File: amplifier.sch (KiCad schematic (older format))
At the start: 3 parts, among them U401 AD8426ACPZ-R7

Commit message: placed digital gnd plane
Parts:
- C401, C402: footprint Capacitor_SMD:C_0805_2012Metric_Pad1.15x1.40mm_HandSolder -> Capacitor_SMD:C_0603_1608Metric_Pad1.05x0.95mm_HandSolder
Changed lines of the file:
@@
 F 0 "C401" H 3615 4846 50  0000 L CNN
 F 1 "0.1uF" H 3615 4755 50  0000 L CNN
-F 2 "Capacitor_SMD:C_0805_2012Metric_Pad1.15x1.40mm_HandSolder" H 3538 4650 50  0001 C CNN
+F 2 "Capacitor_SMD:C_0603_1608Metric_Pad1.05x0.95mm_HandSolder" H 3538 4650 50  0001 C CNN
 F 3 "~" H 3500 4800 50  0001 C CNN
 	1    3500 4800
@@
 F 0 "C402" H 4265 4846 50  0000 L CNN
 F 1 "10uF" H 4265 4755 50  0000 L CNN
-F 2 "Capacitor_SMD:C_0805_2012Metric_Pad1.15x1.40mm_HandSolder" H 4188 4650 50  0001 C CNN
+F 2 "Capacitor_SMD:C_0603_1608Metric_Pad1.05x0.95mm_HandSolder" H 4188 4650 50  0001 C CNN
 F 3 "~" H 4150 4800 50  0001 C CNN
 	1    4150 4800

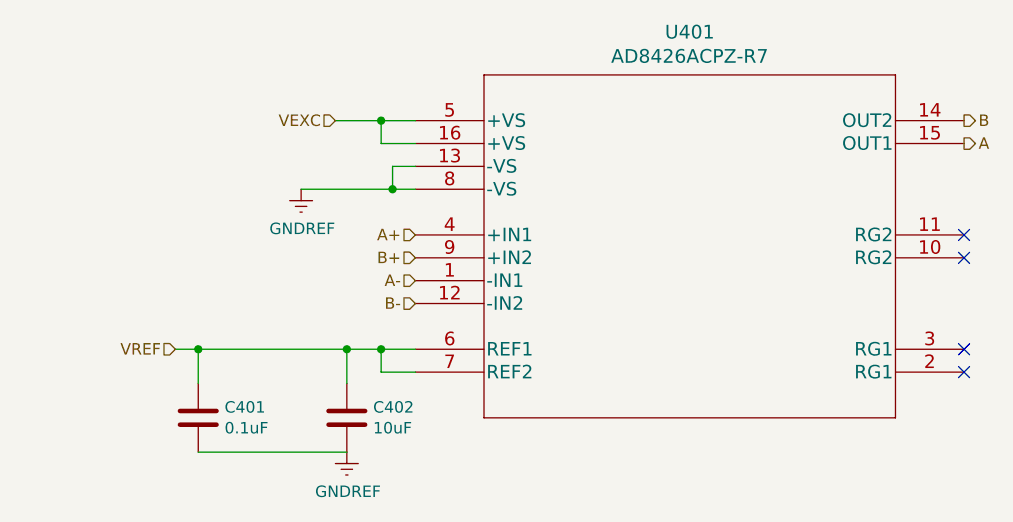
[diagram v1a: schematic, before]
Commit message: without silkscreen
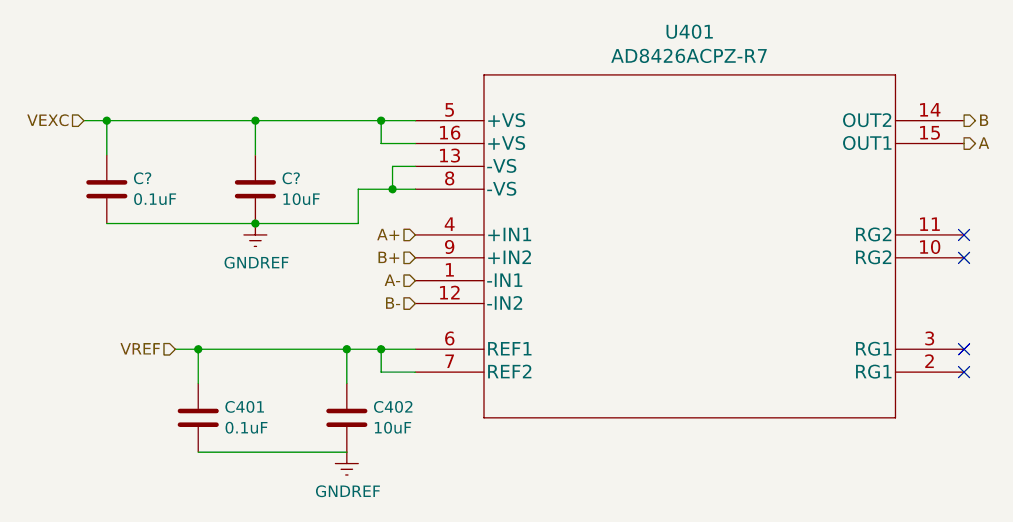
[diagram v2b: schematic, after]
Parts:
- added C?: 0.1uF, Capacitor_SMD:C_0805_2012Metric_Pad1.15x1.40mm_HandSolder, symbol Device:C
- added C?: 10uF, Capacitor_SMD:C_0805_2012Metric_Pad1.15x1.40mm_HandSolder, symbol Device:C
- C401, C402: footprint Capacitor_SMD:C_0603_1608Metric_Pad1.05x0.95mm_HandSolder -> Capacitor_SMD:C_0805_2012Metric_Pad1.15x1.40mm_HandSolder
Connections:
- net GNDREF: now also C?.2, C?.2
- net VEXC: now also C?.1, C?.1
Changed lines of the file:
@@
 Text HLabel 4450 4300 0    50   Input ~ 0
 B-
-Text HLabel 4100 3500 0    50   Input ~ 0
+Text HLabel 3000 3500 0    50   Input ~ 0
 VEXC
-Wire Wire Line
-	4100 3500 4300 3500
 Wire Wire Line
 	4450 3600 4300 3600
@@
 Wire Wire Line
 	4300 3500 4450 3500
-$Comp
-L power:GNDREF #PWR0122
-U 1 1 5F68B73B
-P 3950 3800
-F 0 "#PWR0122" H 3950 3550 50  0001 C CNN
-F 1 "GNDREF" H 3955 3627 50  0000 C CNN
-F 2 "" H 3950 3800 50  0001 C CNN
-F 3 "" H 3950 3800 50  0001 C CNN
-	1    3950 3800
-	1    0    0    -1
-$EndComp
-Wire Wire Line
-	3950 3800 4350 3800
 Wire Wire Line
 	4350 3800 4350 3700
 Wire Wire Line
 	4350 3700 4450 3700
-Connection ~ 4350 3800
 Wire Wire Line
 	4350 3800 4450 3800
@@
 F 0 "C401" H 3615 4846 50  0000 L CNN
 F 1 "0.1uF" H 3615 4755 50  0000 L CNN
-F 2 "Capacitor_SMD:C_0603_1608Metric_Pad1.05x0.95mm_HandSolder" H 3538 4650 50  0001 C CNN
+F 2 "Capacitor_SMD:C_0805_2012Metric_Pad1.15x1.40mm_HandSolder" H 3538 4650 50  0001 C CNN
 F 3 "~" H 3500 4800 50  0001 C CNN
 	1    3500 4800
@@
 F 0 "C402" H 4265 4846 50  0000 L CNN
 F 1 "10uF" H 4265 4755 50  0000 L CNN
-F 2 "Capacitor_SMD:C_0603_1608Metric_Pad1.05x0.95mm_HandSolder" H 4188 4650 50  0001 C CNN
+F 2 "Capacitor_SMD:C_0805_2012Metric_Pad1.15x1.40mm_HandSolder" H 4188 4650 50  0001 C CNN
 F 3 "~" H 4150 4800 50  0001 C CNN
 	1    4150 4800
@@
 Wire Wire Line
 	3500 4950 4150 4950
+$Comp
+L Device:C C?
+U 1 1 5F8A8C07
+P 3100 3800
+F 0 "C?" H 3215 3846 50  0000 L CNN
+F 1 "0.1uF" H 3215 3755 50  0000 L CNN
+F 2 "Capacitor_SMD:C_0805_2012Metric_Pad1.15x1.40mm_HandSolder" H 3138 3650 50  0001 C CNN
+F 3 "~" H 3100 3800 50  0001 C CNN
+	1    3100 3800
+	1    0    0    -1
+$EndComp
+$Comp
+L Device:C C?
+U 1 1 5F8A8C0D
+P 3750 3800
+F 0 "C?" H 3865 3846 50  0000 L CNN
+F 1 "10uF" H 3865 3755 50  0000 L CNN
+F 2 "Capacitor_SMD:C_0805_2012Metric_Pad1.15x1.40mm_HandSolder" H 3788 3650 50  0001 C CNN
+F 3 "~" H 3750 3800 50  0001 C CNN
+	1    3750 3800
+	1    0    0    -1
+$EndComp
+Wire Wire Line
+	3750 3650 3750 3500
+Connection ~ 3750 3500
+Wire Wire Line
+	3100 3650 3100 3500
+Wire Wire Line
+	3000 3500 3100 3500
+Connection ~ 3100 3500
+Wire Wire Line
+	3100 3500 3750 3500
+Wire Wire Line
+	3100 3950 3750 3950
+Wire Wire Line
+	3750 3500 4300 3500
+Wire Wire Line
+	4350 3800 4200 3800
+Wire Wire Line
+	4200 3800 4200 3950
+Wire Wire Line
+	4200 3950 3750 3950
+Connection ~ 4350 3800
+Connection ~ 3750 3950
+$Comp
+L power:GNDREF #PWR?
+U 1 1 5F8B3B5B
+P 3750 3950
+F 0 "#PWR?" H 3750 3700 50  0001 C CNN
+F 1 "GNDREF" H 3755 3777 50  0000 C CNN
+F 2 "" H 3750 3950 50  0001 C CNN
+F 3 "" H 3750 3950 50  0001 C CNN
+	1    3750 3950
+	1    0    0    -1
+$EndComp
 $EndSCHEMATC

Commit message: update website
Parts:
- gave numbers to parts that had none: 2
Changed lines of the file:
@@
 	3500 4950 4150 4950
 $Comp
-L Device:C C?
+L Device:C C403
 U 1 1 5F8A8C07
 P 3100 3800
-F 0 "C?" H 3215 3846 50  0000 L CNN
+F 0 "C403" H 3215 3846 50  0000 L CNN
 F 1 "0.1uF" H 3215 3755 50  0000 L CNN
 F 2 "Capacitor_SMD:C_0805_2012Metric_Pad1.15x1.40mm_HandSolder" H 3138 3650 50  0001 C CNN
@@
 $EndComp
 $Comp
-L Device:C C?
+L Device:C C404
 U 1 1 5F8A8C0D
 P 3750 3800
-F 0 "C?" H 3865 3846 50  0000 L CNN
+F 0 "C404" H 3865 3846 50  0000 L CNN
 F 1 "10uF" H 3865 3755 50  0000 L CNN
 F 2 "Capacitor_SMD:C_0805_2012Metric_Pad1.15x1.40mm_HandSolder" H 3788 3650 50  0001 C CNN
@@
 Connection ~ 3750 3950
 $Comp
-L power:GNDREF #PWR?
+L power:GNDREF #PWR0113
 U 1 1 5F8B3B5B
 P 3750 3950
-F 0 "#PWR?" H 3750 3700 50  0001 C CNN
+F 0 "#PWR0113" H 3750 3700 50  0001 C CNN
 F 1 "GNDREF" H 3755 3777 50  0000 C CNN
 F 2 "" H 3750 3950 50  0001 C CNN

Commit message: set up for reviewers
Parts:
- C401, C403: LCSC (none) -> C62912
- C402, C404: LCSC (none) -> C46653
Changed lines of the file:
@@
 F 2 "Capacitor_SMD:C_0805_2012Metric_Pad1.15x1.40mm_HandSolder" H 3538 4650 50  0001 C CNN
 F 3 "~" H 3500 4800 50  0001 C CNN
+F 4 "C62912" H 3500 4800 50  0001 C CNN "LCSC"
 	1    3500 4800
 	1    0    0    -1
@@
 F 2 "Capacitor_SMD:C_0805_2012Metric_Pad1.15x1.40mm_HandSolder" H 4188 4650 50  0001 C CNN
 F 3 "~" H 4150 4800 50  0001 C CNN
+F 4 "C46653" H 4150 4800 50  0001 C CNN "LCSC"
 	1    4150 4800
 	1    0    0    -1
@@
 F 2 "Capacitor_SMD:C_0805_2012Metric_Pad1.15x1.40mm_HandSolder" H 3138 3650 50  0001 C CNN
 F 3 "~" H 3100 3800 50  0001 C CNN
+F 4 "C62912" H 3100 3800 50  0001 C CNN "LCSC"
 	1    3100 3800
 	1    0    0    -1
@@
 F 2 "Capacitor_SMD:C_0805_2012Metric_Pad1.15x1.40mm_HandSolder" H 3788 3650 50  0001 C CNN
 F 3 "~" H 3750 3800 50  0001 C CNN
+F 4 "C46653" H 3750 3800 50  0001 C CNN "LCSC"
 	1    3750 3800
 	1    0    0    -1
